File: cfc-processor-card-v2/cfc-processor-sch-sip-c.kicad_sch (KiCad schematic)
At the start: 74 parts, among them J6 DM3BT-DSF-PEJS, U11 TCAN330, U2 DS90CR218AMTD/NOPB, U3 SFEM016GB1EA1TO-I-GE-121-STD, U7 OSD3358-1G-ISM

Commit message: CFC processor schematic Change
changed to hierarchy view, changed all global net labels to hierarchy labels, changed all resistor, capacitor, and ground symbols to modern oresat labels. Deleted connectors sheet and added .history to gitignore.
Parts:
- removed C1, C16, C17, C20, C28, C7: 1n, oresat-passives:0402-C-NOSILK, symbol cfc-card-eagle-import:C-EU0402-C-NOSILK
- removed C21, C23, C24, C25, C26, C27: 10n, oresat-passives:0402-C-NOSILK, symbol cfc-card-eagle-import:C-EU0402-C-NOSILK
- removed C42, C43, C45, C46, C47, C48: 100n, oresat-passives:0402-C-NOSILK, symbol cfc-card-eagle-import:C-EU0402-C-NOSILK
- removed C49: 10u, oresat-passives:0805-C-NOSILK, symbol cfc-card-eagle-import:C-EU0603-C-NOSILK
- removed JP1: JUMPER-SMT_2_NC_TRACE_SILK, cfc-card:SMT-JUMPER_2_NC_TRACE_SILK, symbol cfc-card-eagle-import:JUMPER-SMT_2_NC_TRACE_SILK
- removed R29, R30, R6, R7: 100, oresat-passives:0402-C-NOSILK, symbol cfc-card-eagle-import:R-US_0402-C-NOSILK
- removed U2: DS90CR218AMTD/NOPB, cfc-card:MTD48_TEX-L, symbol cfc-card-eagle-import:DS90CR218AMTD/NOPBMTD48_TEX-L
- C23: renamed from C8; symbol cfc-card-eagle-import:C-EU0805-B -> Device:C_Small
- C24: renamed from C11; symbol cfc-card-eagle-import:C-EU0603-A -> Device:C_Small
- C25: renamed from C31; symbol cfc-card-eagle-import:C-EU0603-A -> Device:C_Small
- C26: renamed from C12; symbol cfc-card-eagle-import:C-EU0603-A -> Device:C_Small
- C27: renamed from C10; symbol cfc-card-eagle-import:C-EU0603-A -> Device:C_Small
- C28: renamed from C9; symbol cfc-card-eagle-import:C-EU0603-A -> Device:C_Small
- C29: renamed from C6; symbol cfc-card-eagle-import:C-EU0603-A -> Device:C_Small
- C30: renamed from C5; symbol cfc-card-eagle-import:C-EU0603-A -> Device:C_Small
- C31: renamed from C3; symbol cfc-card-eagle-import:C-EU0603-A -> Device:C_Small
- C32: renamed from C2; symbol cfc-card-eagle-import:C-EU0805-B -> Device:C_Small
- R54: renamed from R11; symbol cfc-card-eagle-import:R-US_0603-A -> Device:R_Small_US
- R55: renamed from R2; symbol cfc-card-eagle-import:R-US_0603-A -> Device:R_Small_US
- R56: renamed from R3; symbol cfc-card-eagle-import:R-US_0603-A -> Device:R_Small_US
- R57: renamed from R4; symbol cfc-card-eagle-import:R-US_0603-A -> Device:R_Small_US
- R58: renamed from R5; symbol cfc-card-eagle-import:R-US_0603-A -> Device:R_Small_US
- renumbered D2 to D5, D3 to D6, D4 to D7, D5 to D8, J6 to J5, TP22 to TP56, TP30 to TP57, TP29 to TP58, TP28 to TP59, TP27 to TP60, TP26 to TP61, TP24 to TP62, TP23 to TP63, TP21 to TP64, TP20 to TP65, TP19 to TP66, TP32 to TP67, TP31 to TP68, TP1 to TP69, TP18 to TP70, TP4 to TP71, TP13 to TP72, TP40 to TP73, TP35 to TP74, TP9 to TP75, TP10 to TP76, TP11 to TP77, TP14 to TP78, U3 to U12
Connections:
- net UART0_RX renamed UART-RX
- net UART0_TX renamed UART-TX
- no-connect marks 46 -> 32
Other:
- note removed: "DESERIALIZER"
- note removed: "Only need to connect 7 bits + clock"

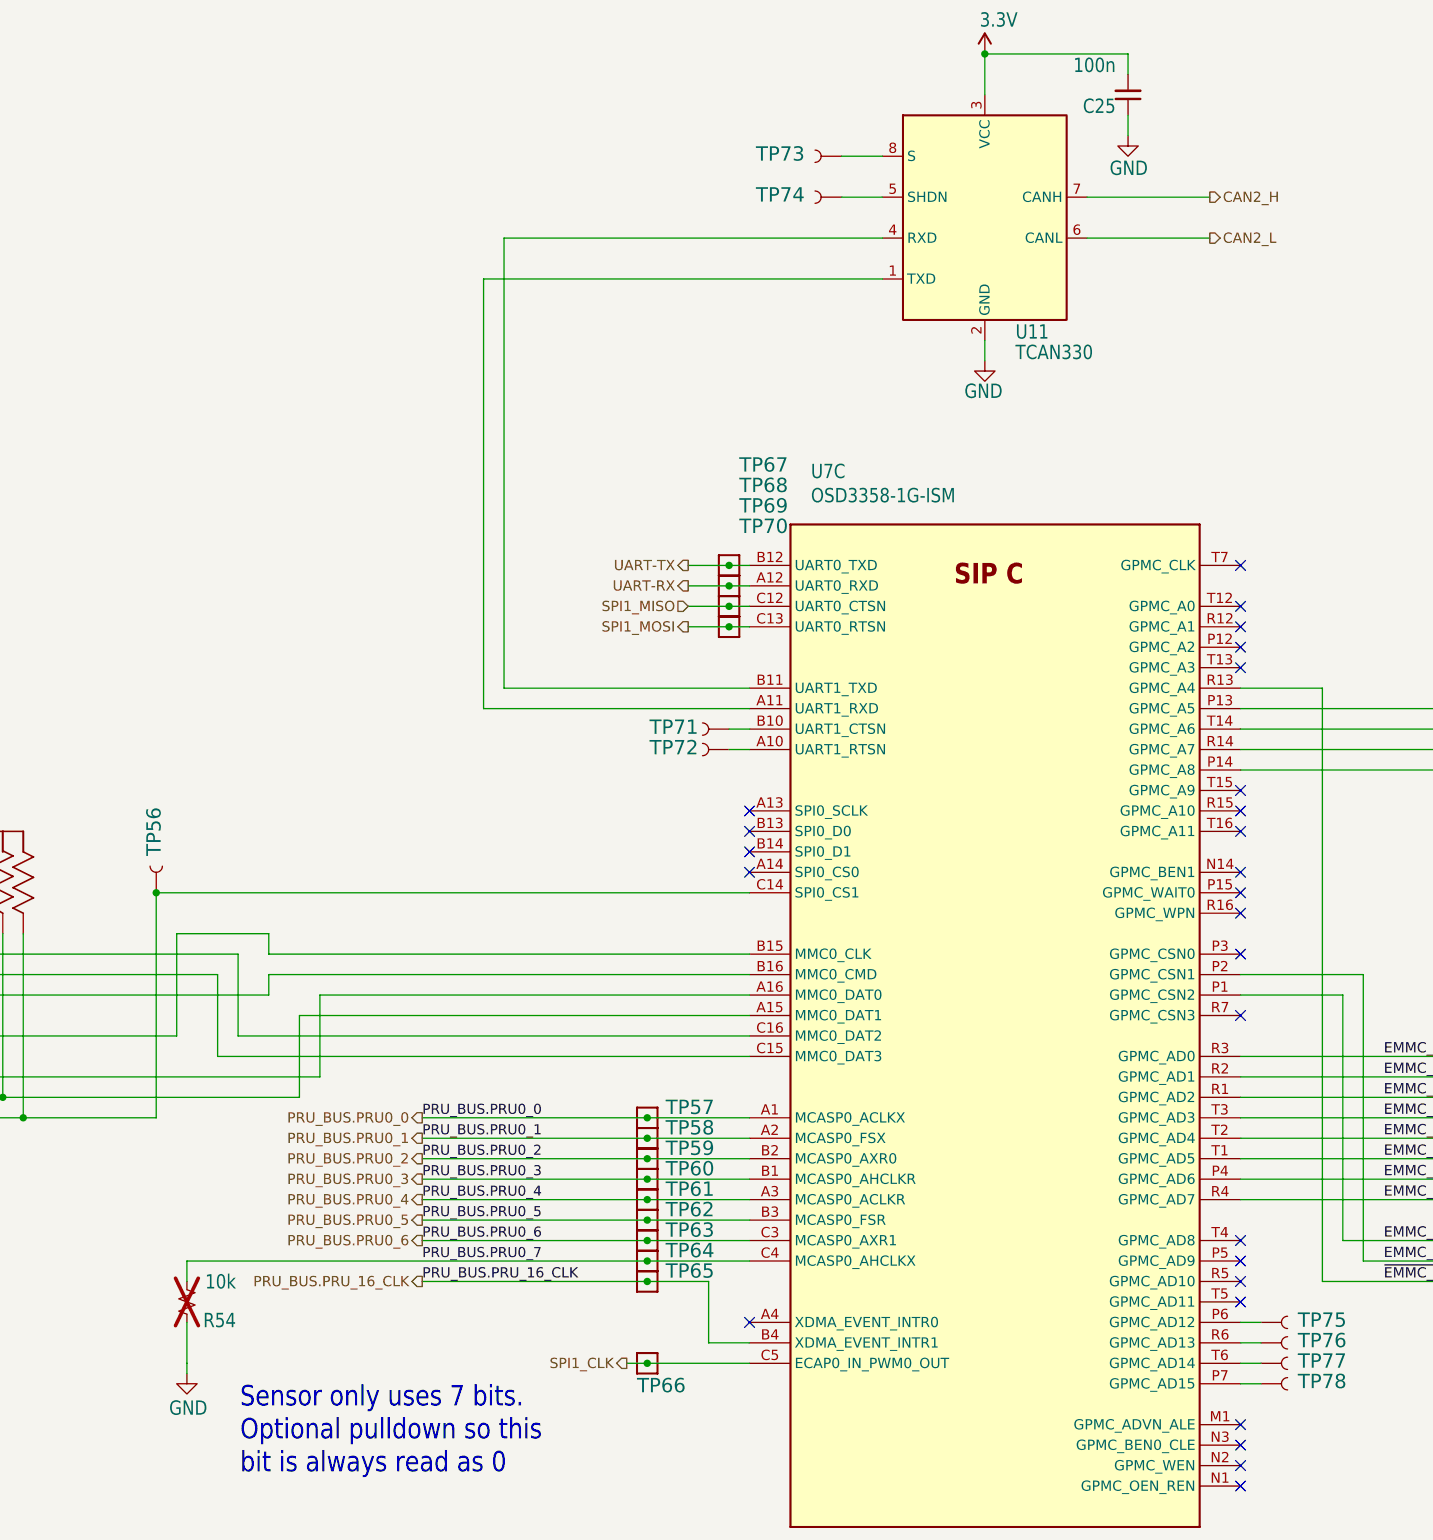
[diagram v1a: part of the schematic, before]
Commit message: Updated OPD
couple of resistors and caps added to schematic. Changed USB ESD clamp VDD to 3.3v instead of octavo created VDD line.
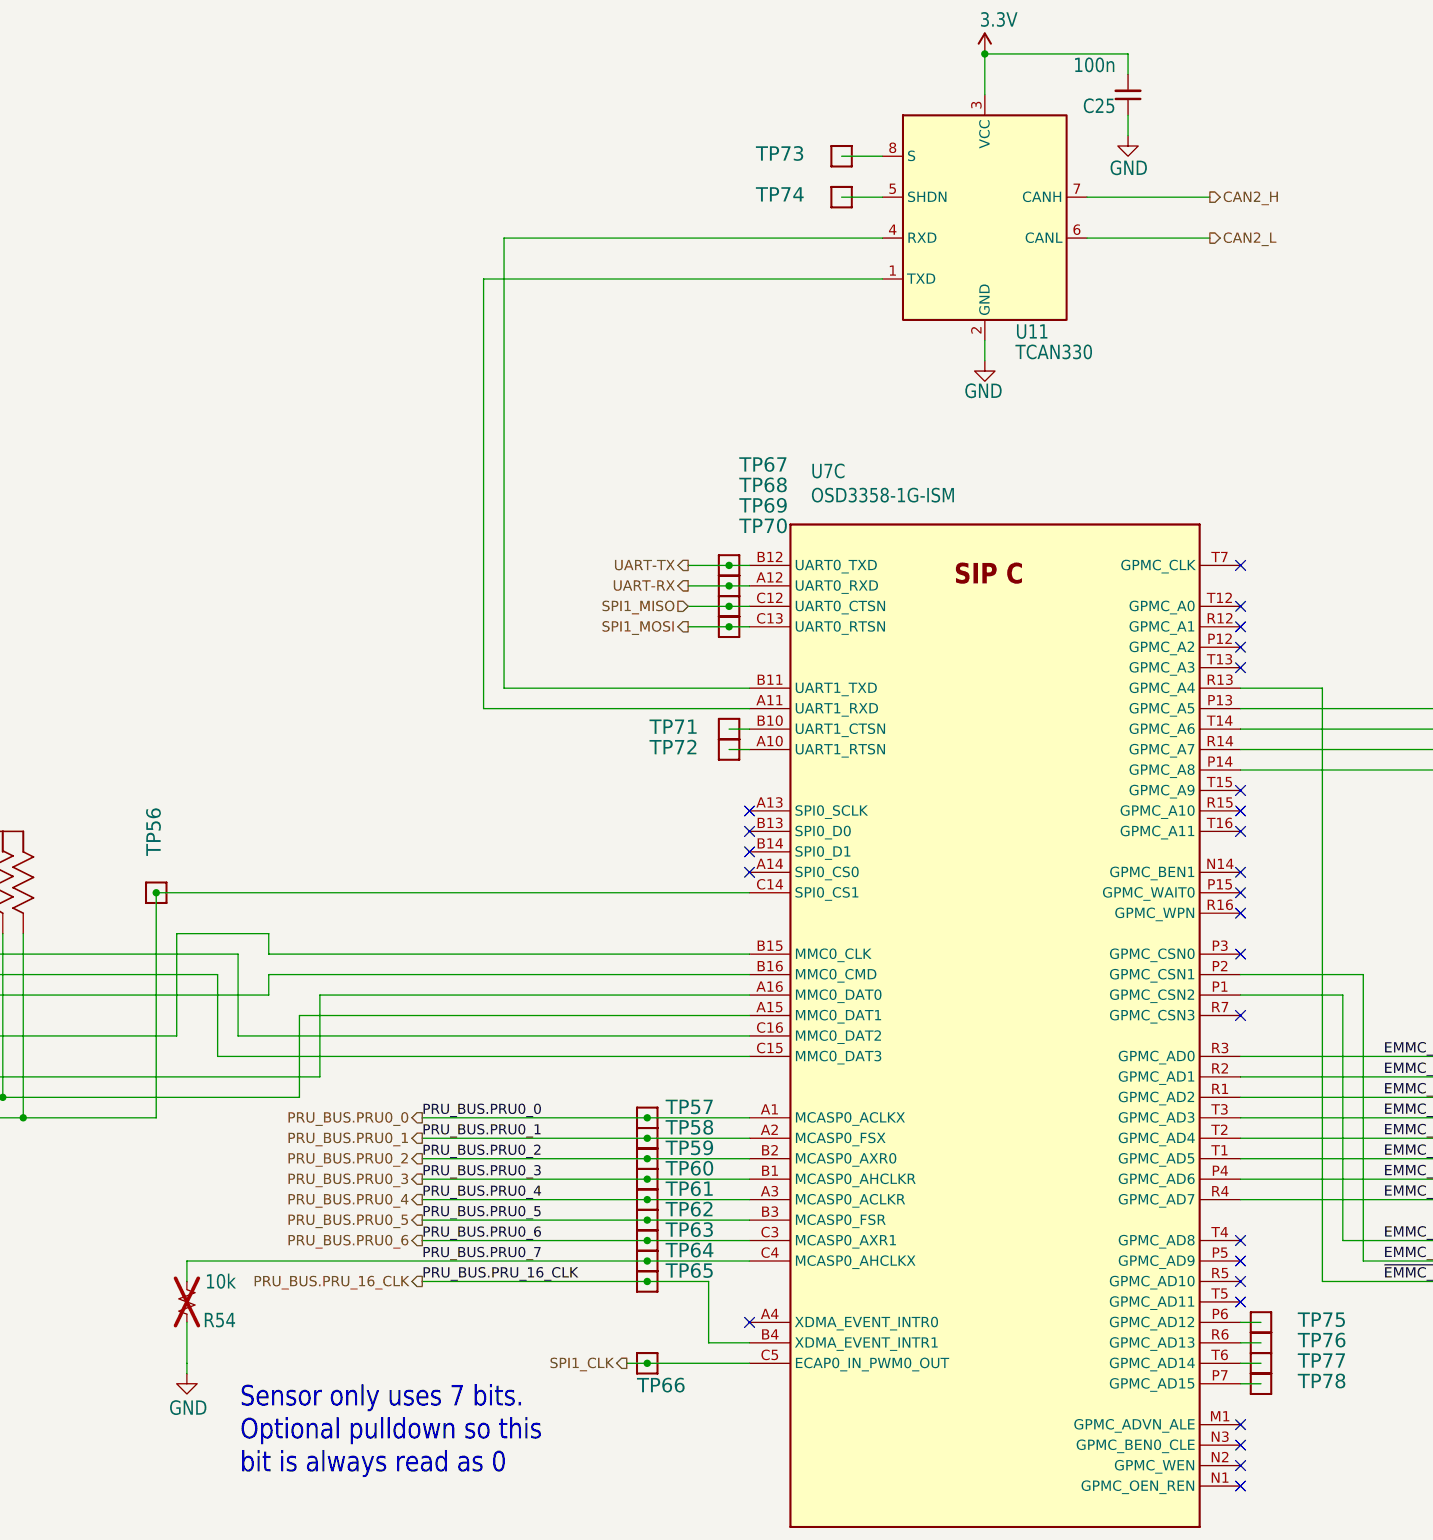
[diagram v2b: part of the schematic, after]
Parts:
- TP56, TP71, TP72, TP73, TP74, TP75, TP76, TP77, TP78: footprint cfc-card:PAD.03X.04 -> oresat-misc:TestPoint_Pad_D1.0mm; symbol cfc-card-eagle-import:TEST-POINT3X4 -> Oresat Misc:Test-Point-1mm-round
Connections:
- net at U11.8 (S): now also TP73.1; no longer TP73.P$1 (1)
- net at U11.5 (SHDN): now also TP74.1; no longer TP74.P$1 (1)
- net at J5.CD (CD#), RA1.6 (66), U7.C14 (SPI0_CS1): now also TP56.1; no longer TP56.P$1 (1)
- net at U7.R6 (GPMC_AD13): now also TP76.1; no longer TP76.P$1 (1)
- net at U7.P6 (GPMC_AD12): now also TP75.1; no longer TP75.P$1 (1)
- net at U7.T6 (GPMC_AD14): now also TP77.1; no longer TP77.P$1 (1)
- net at U7.A10 (UART1_RTSN): now also TP72.1; no longer TP72.P$1 (1)
- net at U7.P7 (GPMC_AD15): now also TP78.1; no longer TP78.P$1 (1)
- net at U7.B10 (UART1_CTSN): now also TP71.1; no longer TP71.P$1 (1)
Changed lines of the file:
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@@
 	)
 	(symbol
-		(lib_id "cfc-card-eagle-import:TEST-POINT3X4")
+		(lib_id "Oresat Misc:Test-Point-1mm-round")
 		(at 199.39 40.64 0)
 		(mirror y)
@@
 			)
 		)
-		(property "Footprint" "cfc-card:PAD.03X.04"
-			(at 199.39 40.64 0)
+		(property "Footprint" "oresat-misc:TestPoint_Pad_D1.0mm"
+			(at 199.39 30.48 0)
 			(hide yes)
 			(show_name no)
@@
 			)
 		)
-		(property "Description" "SparkFun Test Points\n\nBare copper test points for troubleshooting or In-Circuit-Testing. These are used by our Production team for verifying production board runs using pogo-pins on test beds.\n\nSparkFun Products:\n\n• SparkFun LSM9DS1 Breakout\n• SparkFun PSOC\n• https://www.sparkfun.com/products/13879 SparkFun Load Cell Amplifier"
+		(property "Description" "1mm round SMT test point"
 			(at 199.39 40.64 0)
 			(hide yes)
@@
 			)
 		)
-		(pin "P$1"
+		(pin "1"
 		)
 		(instances
@@
 	)
 	(symbol
-		(lib_id "cfc-card-eagle-import:TEST-POINT3X4")
+		(lib_id "Oresat Misc:Test-Point-1mm-round")
 		(at 251.46 187.96 0)
 		(unit 1)
@@
 			)
 		)
-		(property "Footprint" "cfc-card:PAD.03X.04"
-			(at 251.46 187.96 0)
+		(property "Footprint" "oresat-misc:TestPoint_Pad_D1.0mm"
+			(at 251.46 177.8 0)
 			(hide yes)
 			(show_name no)
@@
 			)
 		)
-		(property "Description" "SparkFun Test Points\n\nBare copper test points for troubleshooting or In-Circuit-Testing. These are used by our Production team for verifying production board runs using pogo-pins on test beds.\n\nSparkFun Products:\n\n• SparkFun LSM9DS1 Breakout\n• SparkFun PSOC\n• https://www.sparkfun.com/products/13879 SparkFun Load Cell Amplifier"
+		(property "Description" "1mm round SMT test point"
 			(at 251.46 187.96 0)
 			(hide yes)
@@
 			)
 		)
-		(pin "P$1"
+		(pin "1"
 		)
 		(instances
@@
 	)
 	(symbol
-		(lib_id "cfc-card-eagle-import:TEST-POINT3X4")
+		(lib_id "Oresat Misc:Test-Point-1mm-round")
 		(at 251.46 185.42 0)
 		(unit 1)
@@
 			)
 		)
-		(property "Footprint" "cfc-card:PAD.03X.04"
-			(at 251.46 185.42 0)
+		(property "Footprint" "oresat-misc:TestPoint_Pad_D1.0mm"
+			(at 251.46 175.26 0)
 			(hide yes)
 			(show_name no)
@@
 			)
 		)
-		(property "Description" "SparkFun Test Points\n\nBare copper test points for troubleshooting or In-Circuit-Testing. These are used by our Production team for verifying production board runs using pogo-pins on test beds.\n\nSparkFun Products:\n\n• SparkFun LSM9DS1 Breakout\n• SparkFun PSOC\n• https://www.sparkfun.com/products/13879 SparkFun Load Cell Amplifier"
+		(property "Description" "1mm round SMT test point"
 			(at 251.46 185.42 0)
 			(hide yes)
@@
 			)
 		)
-		(pin "P$1"
+		(pin "1"
 		)
 		(instances
@@
 	)
 	(symbol
-		(lib_id "cfc-card-eagle-import:TEST-POINT3X4")
+		(lib_id "Oresat Misc:Test-Point-1mm-round")
 		(at 251.46 190.5 0)
 		(unit 1)
@@
 			)
 		)
-		(property "Footprint" "cfc-card:PAD.03X.04"
-			(at 251.46 190.5 0)
+		(property "Footprint" "oresat-misc:TestPoint_Pad_D1.0mm"
+			(at 251.46 180.34 0)
 			(hide yes)
 			(show_name no)
@@
 			)
 		)
-		(property "Description" "SparkFun Test Points\n\nBare copper test points for troubleshooting or In-Circuit-Testing. These are used by our Production team for verifying production board runs using pogo-pins on test beds.\n\nSparkFun Products:\n\n• SparkFun LSM9DS1 Breakout\n• SparkFun PSOC\n• https://www.sparkfun.com/products/13879 SparkFun Load Cell Amplifier"
+		(property "Description" "1mm round SMT test point"
 			(at 251.46 190.5 0)
 			(hide yes)
@@
 			)
 		)
-		(pin "P$1"
+		(pin "1"
 		)
 		(instances
@@
 	)
 	(symbol
-		(lib_id "cfc-card-eagle-import:TEST-POINT3X4")
+		(lib_id "Oresat Misc:Test-Point-1mm-round")
 		(at 199.39 45.72 0)
 		(mirror y)
@@
 			)
 		)
-		(property "Footprint" "cfc-card:PAD.03X.04"
-			(at 199.39 45.72 0)
+		(property "Footprint" "oresat-misc:TestPoint_Pad_D1.0mm"
+			(at 199.39 35.56 0)
 			(hide yes)
 			(show_name no)
@@
 			)
 		)
-		(property "Description" "SparkFun Test Points\n\nBare copper test points for troubleshooting or In-Circuit-Testing. These are used by our Production team for verifying production board runs using pogo-pins on test beds.\n\nSparkFun Products:\n\n• SparkFun LSM9DS1 Breakout\n• SparkFun PSOC\n• https://www.sparkfun.com/products/13879 SparkFun Load Cell Amplifier"
+		(property "Description" "1mm round SMT test point"
 			(at 199.39 45.72 0)
 			(hide yes)
@@
 			)
 		)
-		(pin "P$1"
+		(pin "1"
 		)
 		(instances
@@
 	)
 	(symbol
-		(lib_id "cfc-card-eagle-import:TEST-POINT3X4")
+		(lib_id "Oresat Misc:Test-Point-1mm-round")
 		(at 185.42 114.3 180)
 		(unit 1)
@@
 			)
 		)
-		(property "Footprint" "cfc-card:PAD.03X.04"
-			(at 185.42 114.3 0)
+		(property "Footprint" "oresat-misc:TestPoint_Pad_D1.0mm"
+			(at 185.42 124.46 0)
 			(hide yes)
 			(show_name no)
@@
 			)
 		)
-		(property "Description" "SparkFun Test Points\n\nBare copper test points for troubleshooting or In-Circuit-Testing. These are used by our Production team for verifying production board runs using pogo-pins on test beds.\n\nSparkFun Products:\n\n• SparkFun LSM9DS1 Breakout\n• SparkFun PSOC\n• https://www.sparkfun.com/products/13879 SparkFun Load Cell Amplifier"
+		(property "Description" "1mm round SMT test point"
 			(at 185.42 114.3 0)
 			(hide yes)
@@
 			)
 		)
-		(pin "P$1"
+		(pin "1"
 		)
 		(instances
@@
 	)
 	(symbol
-		(lib_id "cfc-card-eagle-import:TEST-POINT3X4")
+		(lib_id "Oresat Misc:Test-Point-1mm-round")
 		(at 114.3 132.08 90)
 		(unit 1)
@@
 			)
 		)
-		(property "Footprint" "cfc-card:PAD.03X.04"
-			(at 114.3 132.08 0)
+		(property "Footprint" "oresat-misc:TestPoint_Pad_D1.0mm"
+			(at 104.14 132.08 0)
 			(hide yes)
 			(show_name no)
@@
 			)
 		)
-		(property "Description" "SparkFun Test Points\n\nBare copper test points for troubleshooting or In-Circuit-Testing. These are used by our Production team for verifying production board runs using pogo-pins on test beds.\n\nSparkFun Products:\n\n• SparkFun LSM9DS1 Breakout\n• SparkFun PSOC\n• https://www.sparkfun.com/products/13879 SparkFun Load Cell Amplifier"
+		(property "Description" "1mm round SMT test point"
 			(at 114.3 132.08 0)
 			(hide yes)
@@
 			)
 		)
-		(pin "P$1"
+		(pin "1"
 		)
 		(instances
@@
 	)
 	(symbol
-		(lib_id "cfc-card-eagle-import:TEST-POINT3X4")
+		(lib_id "Oresat Misc:Test-Point-1mm-round")
 		(at 251.46 193.04 0)
 		(unit 1)
@@
 			)
 		)
-		(property "Footprint" "cfc-card:PAD.03X.04"
-			(at 251.46 193.04 0)
+		(property "Footprint" "oresat-misc:TestPoint_Pad_D1.0mm"
+			(at 251.46 182.88 0)
 			(hide yes)
 			(show_name no)
@@
 			)
 		)
-		(property "Description" "SparkFun Test Points\n\nBare copper test points for troubleshooting or In-Circuit-Testing. These are used by our Production team for verifying production board runs using pogo-pins on test beds.\n\nSparkFun Products:\n\n• SparkFun LSM9DS1 Breakout\n• SparkFun PSOC\n• https://www.sparkfun.com/products/13879 SparkFun Load Cell Amplifier"
+		(property "Description" "1mm round SMT test point"
 			(at 251.46 193.04 0)
 			(hide yes)
@@
 			)
 		)
-		(pin "P$1"
+		(pin "1"
 		)
 		(instances
@@
 	)
 	(symbol
-		(lib_id "cfc-card-eagle-import:TEST-POINT3X4")
+		(lib_id "Oresat Misc:Test-Point-1mm-round")
 		(at 185.42 111.76 180)
 		(unit 1)
@@
 			)
 		)
-		(property "Footprint" "cfc-card:PAD.03X.04"
-			(at 185.42 111.76 0)
+		(property "Footprint" "oresat-misc:TestPoint_Pad_D1.0mm"
+			(at 185.42 121.92 0)
 			(hide yes)
 			(show_name no)
@@
 			)
 		)
-		(property "Description" "SparkFun Test Points\n\nBare copper test points for troubleshooting or In-Circuit-Testing. These are used by our Production team for verifying production board runs using pogo-pins on test beds.\n\nSparkFun Products:\n\n• SparkFun LSM9DS1 Breakout\n• SparkFun PSOC\n• https://www.sparkfun.com/products/13879 SparkFun Load Cell Amplifier"
+		(property "Description" "1mm round SMT test point"
 			(at 185.42 111.76 0)
 			(hide yes)
@@
 			)
 		)
-		(pin "P$1"
+		(pin "1"
 		)
 		(instances
